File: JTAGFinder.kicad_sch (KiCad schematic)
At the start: 0 parts

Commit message: [ADD] sheet mainboard design schematic
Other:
- added sheet propeller p8x32 (p8x32d40.kicad_sch)
- title: JTAGFinder -> JTAGFinder main board
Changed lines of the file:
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@@
   (paper "A4")
   (title_block
-    (title "JTAGFinder")
+    (title "JTAGFinder main board")
     (date "2023-10-22")
     (rev "001")
     (company "fmaw")
   )
+  (sheet (at 208.28 69.215) (size 33.655 36.83) (fields_autoplaced)
+    (stroke (width 0.1524) (type solid))
+    (fill (color 0 0 0 0.0000))
+    (property "Sheetname" "propeller p8x32" (at 208.28 68.5034 0)
+      (effects (font (size 1.27 1.27)) (justify left bottom))
+    )
+    (property "Sheetfile" "p8x32d40.kicad_sch" (at 208.28 106.6296 0)
+      (effects (font (size 1.27 1.27)) (justify left top))
+    )
+    (instances
+      (project "JTAGFinder"
+        (path "/204d557f-3c83-43db-b1fd-628e15efe3d8" (page "2"))
+      )
+    )
+  )
   (sheet_instances

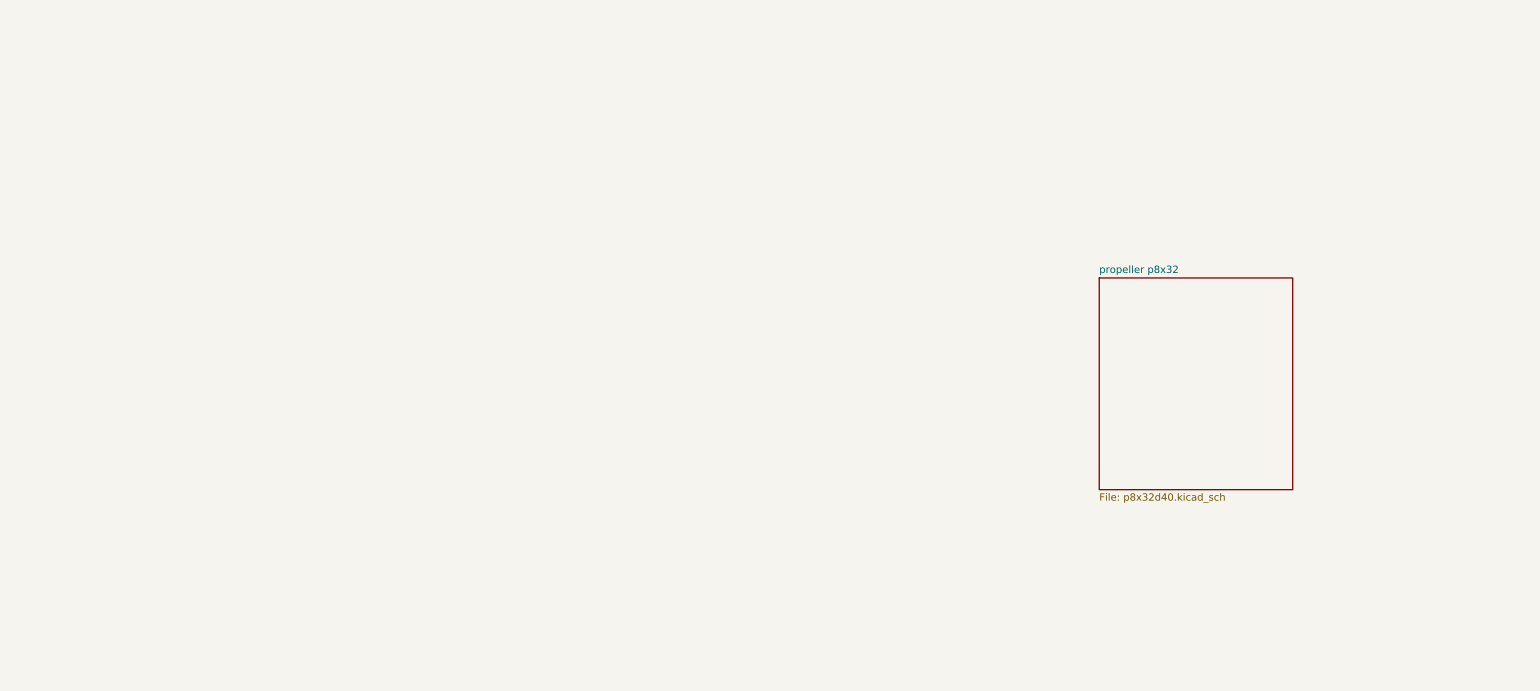
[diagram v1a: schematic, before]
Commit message: [WIP] add sheets for psu + usb interface
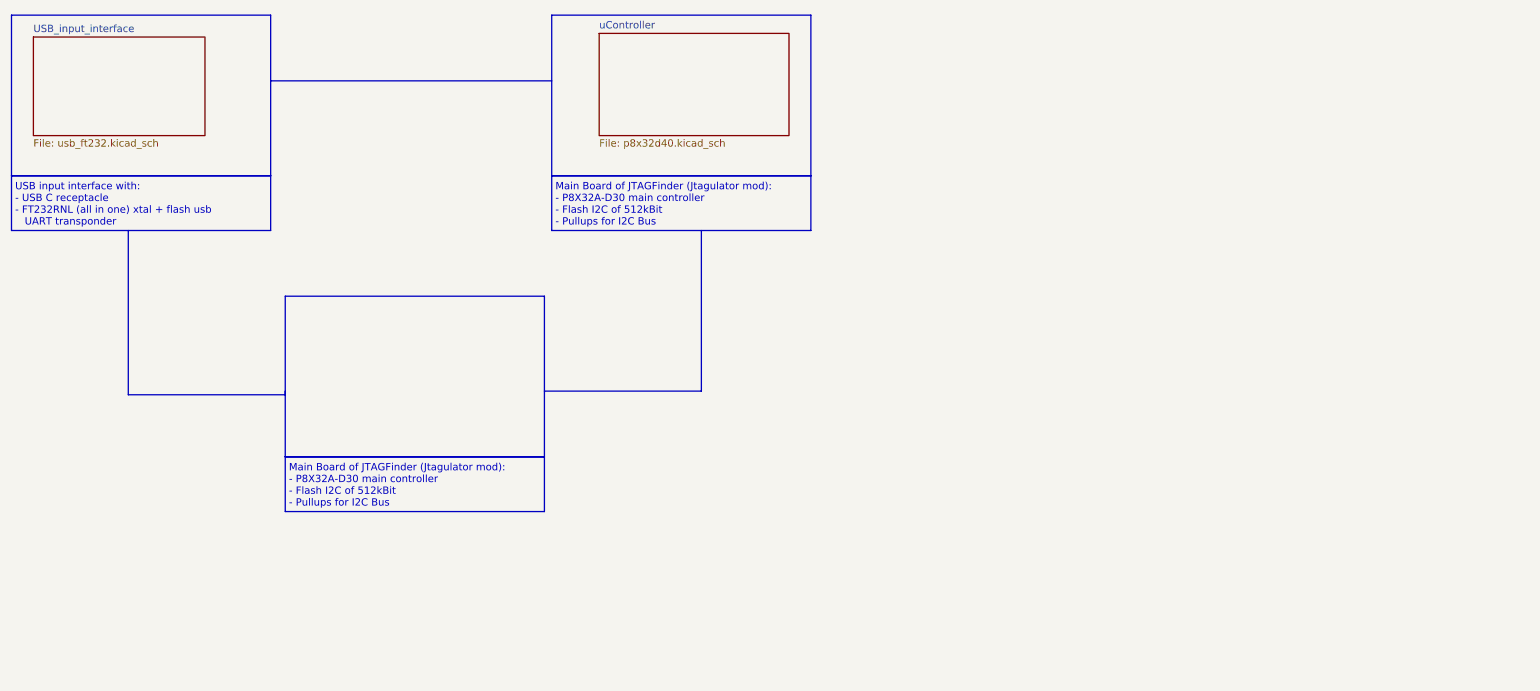
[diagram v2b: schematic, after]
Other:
- sheet propeller p8x32 renamed uController
- added sheet USB_input_interface (usb_ft232.kicad_sch)
- note added: "Main Board of JTAGFinder (Jtagulator mod): - P8X32A-D30 main controller - Flash I2C of 512kBit - Pullups for I2C Bus"
- note added: "USB input interface with: - USB C receptacle - FT232RNL (all in one) xtal + flash usb UART transponder"

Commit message: [WIP] usb connector + ft232RNL
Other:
- added sheet PowerSupply (psu_jtagfinder.kicad_sch)
- note added: "Power Supply: - MIC2025-2YM (dc dc to 5V) - LDO +3V3 - PowerFlags"
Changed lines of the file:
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@@
     (effects (font (size 1.27 1.27)) (justify left bottom))
   )
-  (text "Main Board of JTAGFinder (Jtagulator mod):\n- P8X32A-D30 main controller\n- Flash I2C of 512kBit\n- Pullups for I2C Bus"
+  (text "Power Supply:\n- MIC2025-2YM (dc dc to 5V)\n- LDO +3V3\n- PowerFlags"
     (at 67.31 109.22 0)
     (effects (font (size 1.27 1.27)) (justify left bottom))
@@
     )
   )
-  (sheet (at 121.285 26.67) (size 33.02 17.78) (fields_autoplaced)
+  (sheet (at 118.745 26.67) (size 35.56 22.86)
     (stroke (width 0.1524) (type solid))
     (fill (color 0 0 0 0.0000))
-    (property "Sheetname" "uController" (at 121.285 25.9584 0)
+    (property "Sheetname" "uController" (at 118.745 25.9584 0)
       (effects (font (size 1.27 1.27)) (justify left bottom))
     )
-    (property "Sheetfile" "p8x32d40.kicad_sch" (at 121.285 45.0346 0)
+    (property "Sheetfile" "p8x32d40.kicad_sch" (at 118.745 45.085 0)
       (effects (font (size 1.27 1.27)) (justify left top))
     )
@@
       )
     )
+  )
+  (sheet (at 73.66 79.375) (size 29.845 15.875) (fields_autoplaced)
+    (stroke (width 0.1524) (type solid))
+    (fill (color 0 0 0 0.0000))
+    (property "Sheetname" "PowerSupply" (at 73.66 78.6634 0)
+      (effects (font (size 1.27 1.27)) (justify left bottom))
+    )
+    (property "Sheetfile" "psu_jtagfinder.kicad_sch" (at 73.66 95.8346 0)
+      (effects (font (size 1.27 1.27)) (justify left top))
+    )
+    (instances
+      (project "JTAGFinder"
+        (path "/204d557f-3c83-43db-b1fd-628e15efe3d8" (page "4"))
+      )
+    )

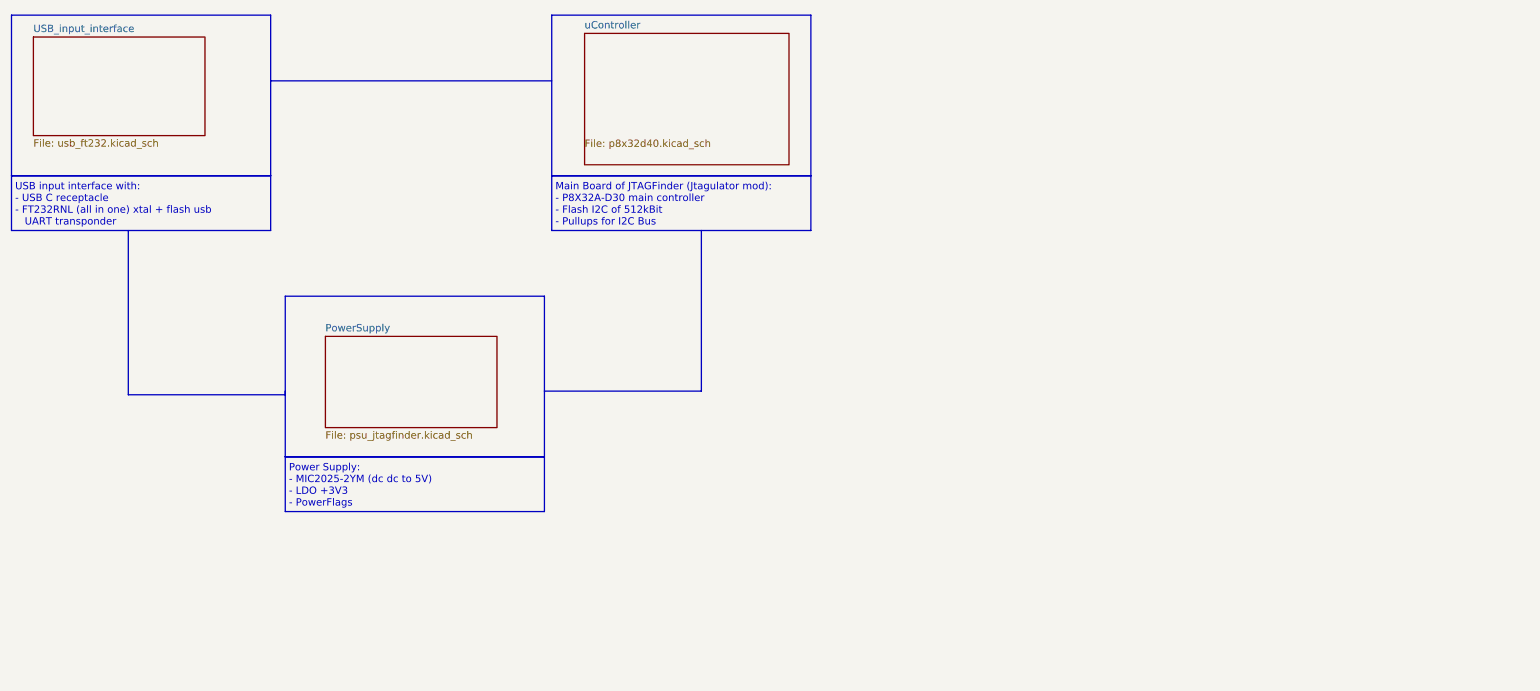
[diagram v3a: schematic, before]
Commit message: [FIX] ERC failure, add sheets for output stage
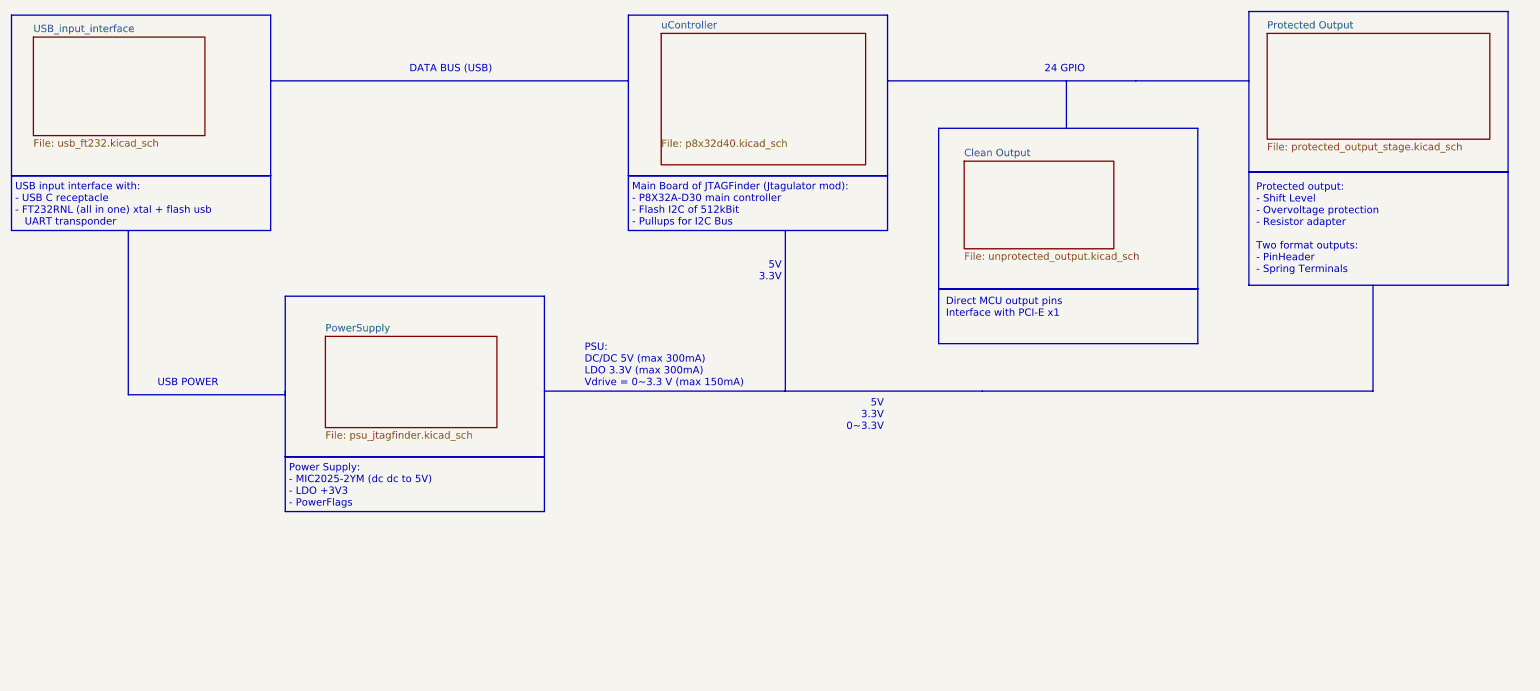
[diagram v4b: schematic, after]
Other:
- added sheet Clean Output (unprotected_output.kicad_sch)
- added sheet Protected Output (protected_output_stage.kicad_sch)
- note added: "24 GPIO"
- note added: "5V 3.3V"
- note added: "5V 3.3V 0~3.3V"
- note added: "DATA BUS (USB)"
- note added: "Direct MCU output pins Interface with PCI-E x1"
- note added: "PSU: DC/DC 5V (max 300mA) LDO 3.3V (max 300mA) Vdrive = 0~3.3 V (max 150mA)"
- note added: "Protected output: - Shift Level - Overvoltage protection - Resistor adapter Two format outputs: - PinHeader - Spring Terminals"
- note added: "USB POWER"
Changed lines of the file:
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@@
     (company "fmaw")
   )
-  (polyline (pts (xy 139.065 60.96) (xy 139.065 88.9))
+  (polyline (pts (xy 153.67 60.96) (xy 153.67 88.9))
     (stroke (width 0) (type default))
   )
@@
     (stroke (width 0) (type default))
   )
-  (polyline (pts (xy 64.135 34.925) (xy 113.03 34.925))
+  (polyline (pts (xy 64.135 34.925) (xy 126.365 34.925))
+    (stroke (width 0) (type default))
+  )
+  (polyline (pts (xy 153.67 88.9) (xy 187.96 88.9))
+    (stroke (width 0) (type default))
+  )
+  (polyline (pts (xy 202.565 34.925) (xy 202.565 43.18))
+    (stroke (width 0) (type default))
+  )
+  (polyline (pts (xy 255.905 70.485) (xy 255.905 88.9))
     (stroke (width 0) (type default))
   )
@@
     (stroke (width 0) (type default))
   )
-  (polyline (pts (xy 111.76 88.9) (xy 139.065 88.9))
+  (polyline (pts (xy 214.63 34.925) (xy 234.315 34.925))
+    (stroke (width 0) (type default))
+  )
+  (polyline (pts (xy 111.76 88.9) (xy 153.67 88.9))
     (stroke (width 0) (type default))
   )
+  (polyline (pts (xy 187.96 88.9) (xy 255.905 88.9))
+    (stroke (width 0) (type default))
+  )
+  (polyline (pts (xy 171.45 34.925) (xy 214.63 34.925))
+    (stroke (width 0) (type default))
+  )
+  (rectangle (start 180.34 43.18) (end 225.425 71.12)
+    (stroke (width 0) (type default))
+    (fill (type none))
+  )
+  (rectangle (start 180.34 71.12) (end 225.425 80.645)
+    (stroke (width 0) (type default))
+    (fill (type none))
+  )
   (rectangle (start 19.05 51.435) (end 64.135 60.96)
     (stroke (width 0) (type default))
     (fill (type none))
   )
-  (rectangle (start 113.03 23.495) (end 158.115 51.435)
+  (rectangle (start 126.365 23.495) (end 171.45 51.435)
+    (stroke (width 0) (type default))
+    (fill (type none))
+  )
+  (rectangle (start 234.315 50.8) (end 279.4 70.485)
     (stroke (width 0) (type default))
     (fill (type none))
@@
     (fill (type none))
   )
-  (rectangle (start 113.03 51.435) (end 158.115 60.96)
+  (rectangle (start 126.365 51.435) (end 171.45 60.96)
     (stroke (width 0) (type default))
     (fill (type none))
@@
     (fill (type none))
   )
+  (rectangle (start 234.315 22.86) (end 279.4 50.8)
+    (stroke (width 0) (type default))
+    (fill (type none))
+  )
   (image (at 29.21 36.195) (scale 0.26866)
     (data
@@
     )
   )
-  (image (at 137.795 35.56) (scale 0.49111)
+  (image (at 151.13 35.56) (scale 0.49111)
     (data
       iVBORw0KGgoAAAANSUhEUgAAAxoAAAGkCAIAAAA5fcQpAAAAA3NCSVQICAjb4U/gAAAACXBIWXMA
@@
   )
   (text "Main Board of JTAGFinder (Jtagulator mod):\n- P8X32A-D30 main controller\n- Flash I2C of 512kBit\n- Pullups for I2C Bus"
-    (at 113.665 60.325 0)
+    (at 127 60.325 0)
+    (effects (font (size 1.27 1.27)) (justify left bottom))
+  )
+  (text "DATA BUS (USB)" (at 88.265 33.655 0)
+    (effects (font (size 1.27 1.27)) (justify left bottom))
+  )
+  (text "5V\n3.3V\n0~3.3V\n" (at 170.815 95.885 0)
+    (effects (font (size 1.27 1.27)) (justify right bottom))
+  )
+  (text "24 GPIO" (at 198.755 33.655 0)
+    (effects (font (size 1.27 1.27)) (justify left bottom))
+  )
+  (text "Direct MCU output pins\nInterface with PCI-E x1" (at 181.61 76.2 0)
     (effects (font (size 1.27 1.27)) (justify left bottom))
   )
+  (text "Protected output:\n- Shift Level\n- Overvoltage protection\n- Resistor adapter\n\nTwo format outputs:\n- PinHeader\n- Spring Terminals"
+    (at 235.585 68.58 0)
+    (effects (font (size 1.27 1.27)) (justify left bottom))
+  )
+  (text "5V\n3.3V" (at 153.035 69.85 0)
+    (effects (font (size 1.27 1.27)) (justify right bottom))
+  )
   (text "Power Supply:\n- MIC2025-2YM (dc dc to 5V)\n- LDO +3V3\n- PowerFlags"
     (at 67.31 109.22 0)
     (effects (font (size 1.27 1.27)) (justify left bottom))
   )
+  (text "USB POWER" (at 44.45 88.265 0)
+    (effects (font (size 1.27 1.27)) (justify left bottom))
+  )
+  (text "PSU:\nDC/DC 5V (max 300mA)\nLDO 3.3V (max 300mA)\nVdrive = 0~3.3 V (max 150mA)"
+    (at 118.745 88.265 0)
+    (effects (font (size 1.27 1.27)) (justify left bottom))
+  )
   (sheet (at 22.86 27.305) (size 29.845 17.145) (fields_autoplaced)
     (stroke (width 0.1524) (type solid))
@@
     )
   )
-  (sheet (at 118.745 26.67) (size 35.56 22.86)
+  (sheet (at 132.08 26.67) (size 35.56 22.86)
     (stroke (width 0.1524) (type solid))
     (fill (color 0 0 0 0.0000))
-    (property "Sheetname" "uController" (at 118.745 25.9584 0)
+    (property "Sheetname" "uController" (at 132.08 25.9584 0)
       (effects (font (size 1.27 1.27)) (justify left bottom))
     )
-    (property "Sheetfile" "p8x32d40.kicad_sch" (at 118.745 45.085 0)
+    (property "Sheetfile" "p8x32d40.kicad_sch" (at 132.08 45.085 0)
       (effects (font (size 1.27 1.27)) (justify left top))
     )
@@
       )
     )
+  )
+  (sheet (at 184.785 48.895) (size 26.035 15.24) (fields_autoplaced)
+    (stroke (width 0.1524) (type solid))
+    (fill (color 0 0 0 0.0000))
+    (property "Sheetname" "Clean Output" (at 184.785 48.1834 0)
+      (effects (font (size 1.27 1.27)) (justify left bottom))
+    )
+    (property "Sheetfile" "unprotected_output.kicad_sch" (at 184.785 64.7196 0)
+      (effects (font (size 1.27 1.27)) (justify left top))
+    )
+    (instances
+      (project "JTAGFinder"
+        (path "/204d557f-3c83-43db-b1fd-628e15efe3d8" (page "6"))
+      )
+    )
+  )
+  (sheet (at 237.49 26.67) (size 38.735 18.415) (fields_autoplaced)
+    (stroke (width 0.1524) (type solid))
+    (fill (color 0 0 0 0.0000))
+    (property "Sheetname" "Protected Output" (at 237.49 25.9584 0)
+      (effects (font (size 1.27 1.27)) (justify left bottom))
+    )
+    (property "Sheetfile" "protected_output_stage.kicad_sch" (at 237.49 45.6696 0)
+      (effects (font (size 1.27 1.27)) (justify left top))
+    )
+    (property "Campo2" "" (at 237.49 26.67 0)
+      (effects (font (size 1.27 1.27)) hide)
+    )
+    (instances
+      (project "JTAGFinder"
+        (path "/204d557f-3c83-43db-b1fd-628e15efe3d8" (page "5"))
+      )
+    )

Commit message: finish update extra updates
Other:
- added sheet extra_interface (extra_interface.kicad_sch)
- note added: "Extra interfaces: - Firmware 3 pin to control HW rev - BT Interface - LCD - KeyPad"
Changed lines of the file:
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@@
     (stroke (width 0) (type default))
   )
+  (polyline (pts (xy 153.67 88.9) (xy 153.67 97.79))
+    (stroke (width 0) (type default))
+  )
+  (rectangle (start 130.81 125.73) (end 175.895 139.065)
+    (stroke (width 0) (type default))
+    (fill (type none))
+  )
   (rectangle (start 180.34 43.18) (end 225.425 71.12)
     (stroke (width 0) (type default))
@@
     (fill (type none))
   )
+  (rectangle (start 130.81 97.79) (end 175.895 125.73)
+    (stroke (width 0) (type default))
+    (fill (type none))
+  )
   (rectangle (start 234.315 50.8) (end 279.4 70.485)
     (stroke (width 0) (type default))
@@
     (effects (font (size 1.27 1.27)) (justify left bottom))
   )
+  (text "Extra interfaces:\n- Firmware 3 pin to control HW rev\n- BT Interface\n- LCD\n- KeyPad"
+    (at 130.81 138.43 0)
+    (effects (font (size 1.27 1.27)) (justify left bottom))
+  )
   (sheet (at 22.86 27.305) (size 29.845 17.145) (fields_autoplaced)
     (stroke (width 0.1524) (type solid))
@@
       )
     )
+  )
+  (sheet (at 138.43 103.505) (size 30.48 13.97) (fields_autoplaced)
+    (stroke (width 0.1524) (type solid))
+    (fill (color 0 0 0 0.0000))
+    (property "Sheetname" "extra_interface" (at 138.43 102.7934 0)
+      (effects (font (size 1.27 1.27)) (justify left bottom))
+    )
+    (property "Sheetfile" "extra_interface.kicad_sch" (at 138.43 118.0596 0)
+      (effects (font (size 1.27 1.27)) (justify left top))
+    )
+    (instances
+      (project "JTAGFinder"
+        (path "/204d557f-3c83-43db-b1fd-628e15efe3d8" (page "7"))
+      )
+    )
